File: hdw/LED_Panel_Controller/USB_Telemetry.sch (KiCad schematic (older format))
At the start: 7 parts

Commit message: reworked some USB stuff
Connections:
- net POS12_SNS+ renamed POS5_USB_SNS+
- net POS12_SNS- renamed POS5_USB_SNS-
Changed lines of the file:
@@
 $Descr A 11000 8500
 encoding utf-8
-Sheet 3 34
+Sheet 34 34
 Title "Pulse Oximeter"
 Date "2020-08-01"
@@
 $EndDescr
 Text GLabel 3790 1800 0    50   UnSpc ~ 0
-POS12_SNS+
+POS5_USB_SNS+
 Text GLabel 3790 2260 0    50   UnSpc ~ 0
-POS12_SNS-
+POS5_USB_SNS-
 $Comp
 L power:GND #PWR?
@@
 AR Path="/5EAE2D84/5E0ACFF2" Ref="#PWR?"  Part="1"
 AR Path="/5F581B58/5E0ACFF2" Ref="#PWR?"  Part="1"
+AR Path="/5F581BB7/5E0ACFF2" Ref="#PWR?"  Part="1"
+AR Path="/5F7B4289/5E0ACFF2" Ref="#PWR?"  Part="1"
 F 0 "#PWR?" H 5110 2190 50  0001 C CNN
 F 1 "GND" H 5110 2290 50  0000 C CNN
@@
 AR Path="/5EAE2D84/5E0AD665" Ref="#PWR?"  Part="1"
 AR Path="/5F581B58/5E0AD665" Ref="#PWR?"  Part="1"
+AR Path="/5F581BB7/5E0AD665" Ref="#PWR?"  Part="1"
+AR Path="/5F7B4289/5E0AD665" Ref="#PWR?"  Part="1"
 F 0 "#PWR?" H 5110 1490 50  0001 C CNN
 F 1 "+3.3V" H 5110 1780 50  0000 C CNN
@@
 AR Path="/5EAE2D84/5E0B2427" Ref="C?"  Part="1"
 AR Path="/5F581B58/5E0B2427" Ref="C?"  Part="1"
+AR Path="/5F581BB7/5E0B2427" Ref="C?"  Part="1"
+AR Path="/5F7B4289/5E0B2427" Ref="C?"  Part="1"
 F 0 "C?" H 5135 3110 50  0000 L CNN
 F 1 "0.1uF" H 5135 2910 50  0000 L CNN
@@
 AR Path="/5EAE2D84/5E0B535B" Ref="#PWR?"  Part="1"
 AR Path="/5F581B58/5E0B535B" Ref="#PWR?"  Part="1"
+AR Path="/5F581BB7/5E0B535B" Ref="#PWR?"  Part="1"
+AR Path="/5F7B4289/5E0B535B" Ref="#PWR?"  Part="1"
 F 0 "#PWR?" H 5110 2710 50  0001 C CNN
 F 1 "+3.3V" H 5110 3000 50  0000 C CNN
@@
 AR Path="/5EAE2D84/5E0B592B" Ref="#PWR?"  Part="1"
 AR Path="/5F581B58/5E0B592B" Ref="#PWR?"  Part="1"
+AR Path="/5F581BB7/5E0B592B" Ref="#PWR?"  Part="1"
+AR Path="/5F7B4289/5E0B592B" Ref="#PWR?"  Part="1"
 F 0 "#PWR?" H 5110 2910 50  0001 C CNN
 F 1 "GND" H 5110 3010 50  0000 C CNN
@@
 AR Path="/5EAE2D84/5E0B8BC8" Ref="DOC?"  Part="1"
 AR Path="/5F581B58/5E0B8BC8" Ref="DOC?"  Part="1"
+AR Path="/5F581BB7/5E0B8BC8" Ref="DOC?"  Part="1"
+AR Path="/5F7B4289/5E0B8BC8" Ref="DOC?"  Part="1"
 F 0 "DOC?" H 6010 3130 60  0001 C CNN
 F 1 "FIXME" H 5560 2880 60  0000 L CNN
@@
 AR Path="/5EAE2D84/5E2AA995" Ref="#PWR?"  Part="1"
 AR Path="/5F581B58/5E2AA995" Ref="#PWR?"  Part="1"
+AR Path="/5F581BB7/5E2AA995" Ref="#PWR?"  Part="1"
+AR Path="/5F7B4289/5E2AA995" Ref="#PWR?"  Part="1"
 F 0 "#PWR?" H 5110 4870 50  0001 C CNN
 F 1 "GND" H 5110 4970 50  0000 C CNN
@@
 AR Path="/5EAE2D84/5E2AA99A" Ref="#PWR?"  Part="1"
 AR Path="/5F581B58/5E2AA99A" Ref="#PWR?"  Part="1"
+AR Path="/5F581BB7/5E2AA99A" Ref="#PWR?"  Part="1"
+AR Path="/5F7B4289/5E2AA99A" Ref="#PWR?"  Part="1"
 F 0 "#PWR?" H 5110 3890 50  0001 C CNN
 F 1 "+3.3V" H 5110 4180 50  0000 C CNN
@@
 AR Path="/5EAE2D84/5E2AA99D" Ref="U?"  Part="1"
 AR Path="/5F581B58/5E2AA99D" Ref="U?"  Part="1"
+AR Path="/5F581BB7/5E2AA99D" Ref="U?"  Part="1"
+AR Path="/5F7B4289/5E2AA99D" Ref="U?"  Part="1"
 F 0 "U?" H 4860 4990 50  0000 C CNN
 F 1 "MCP9804" H 5510 4990 50  0000 C CNN
@@
 AR Path="/5EAE2D84/5E2AA9A1" Ref="C?"  Part="1"
 AR Path="/5F581B58/5E2AA9A1" Ref="C?"  Part="1"
+AR Path="/5F581BB7/5E2AA9A1" Ref="C?"  Part="1"
+AR Path="/5F7B4289/5E2AA9A1" Ref="C?"  Part="1"
 F 0 "C?" H 5135 5790 50  0000 L CNN
 F 1 "0.1uF" H 5135 5590 50  0000 L CNN
@@
 AR Path="/5EAE2D84/5E2AA9A6" Ref="#PWR?"  Part="1"
 AR Path="/5F581B58/5E2AA9A6" Ref="#PWR?"  Part="1"
+AR Path="/5F581BB7/5E2AA9A6" Ref="#PWR?"  Part="1"
+AR Path="/5F7B4289/5E2AA9A6" Ref="#PWR?"  Part="1"
 F 0 "#PWR?" H 5110 5390 50  0001 C CNN
 F 1 "+3.3V" H 5110 5680 50  0000 C CNN
@@
 AR Path="/5EAE2D84/5E2AA9AD" Ref="#PWR?"  Part="1"
 AR Path="/5F581B58/5E2AA9AD" Ref="#PWR?"  Part="1"
+AR Path="/5F581BB7/5E2AA9AD" Ref="#PWR?"  Part="1"
+AR Path="/5F7B4289/5E2AA9AD" Ref="#PWR?"  Part="1"
 F 0 "#PWR?" H 5110 5590 50  0001 C CNN
 F 1 "GND" H 5110 5690 50  0000 C CNN
@@
 AR Path="/5EAE2D84/5E2AA9AF" Ref="DOC?"  Part="1"
 AR Path="/5F581B58/5E2AA9AF" Ref="DOC?"  Part="1"
+AR Path="/5F581BB7/5E2AA9AF" Ref="DOC?"  Part="1"
+AR Path="/5F7B4289/5E2AA9AF" Ref="DOC?"  Part="1"
 F 0 "DOC?" H 6010 5810 60  0001 C CNN
 F 1 "FIXME" H 5560 5560 60  0000 L CNN
@@
 AR Path="/5EAE2D84/5E07E0FD" Ref="C?"  Part="1"
 AR Path="/5F581B58/5E07E0FD" Ref="C?"  Part="1"
+AR Path="/5F581BB7/5E07E0FD" Ref="C?"  Part="1"
+AR Path="/5F7B4289/5E07E0FD" Ref="C?"  Part="1"
 F 0 "C?" H 4255 2130 50  0000 L CNN
 F 1 "0.1uF" H 4255 1930 50  0000 L CNN

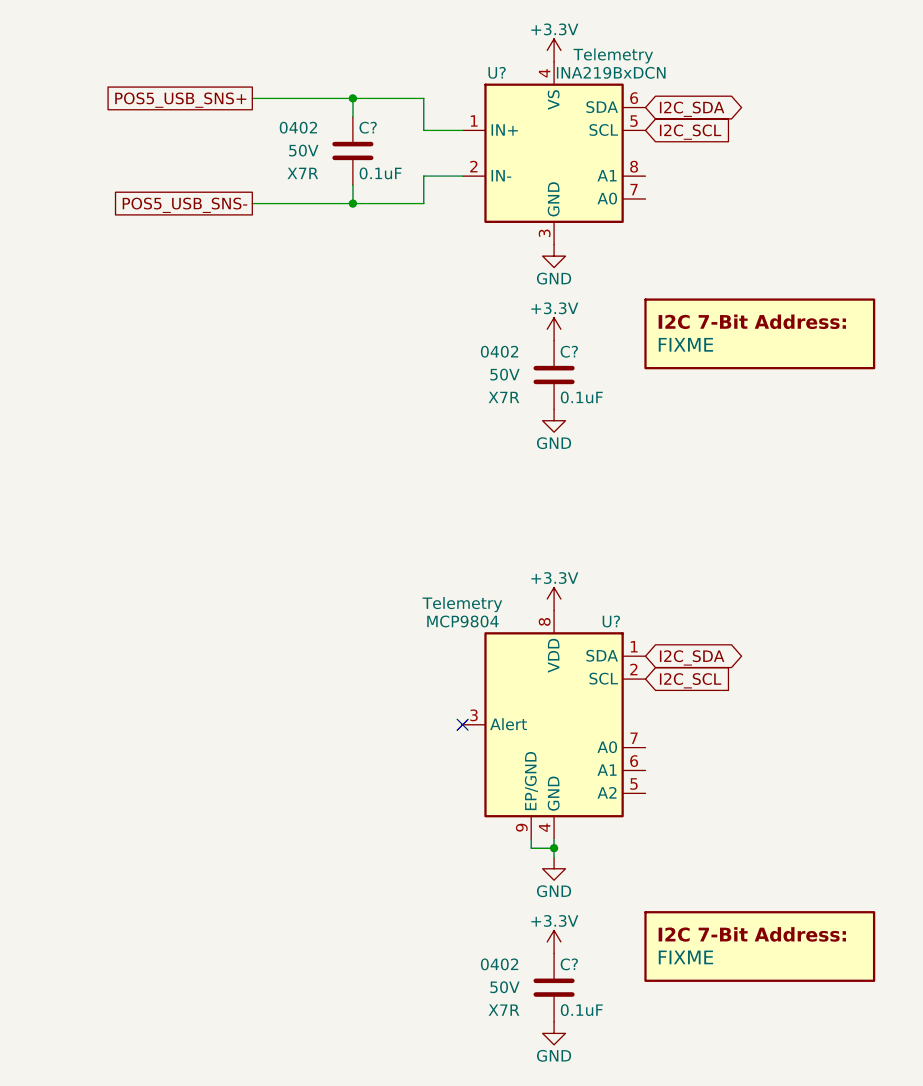
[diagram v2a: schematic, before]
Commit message: fixed level shifter sheet
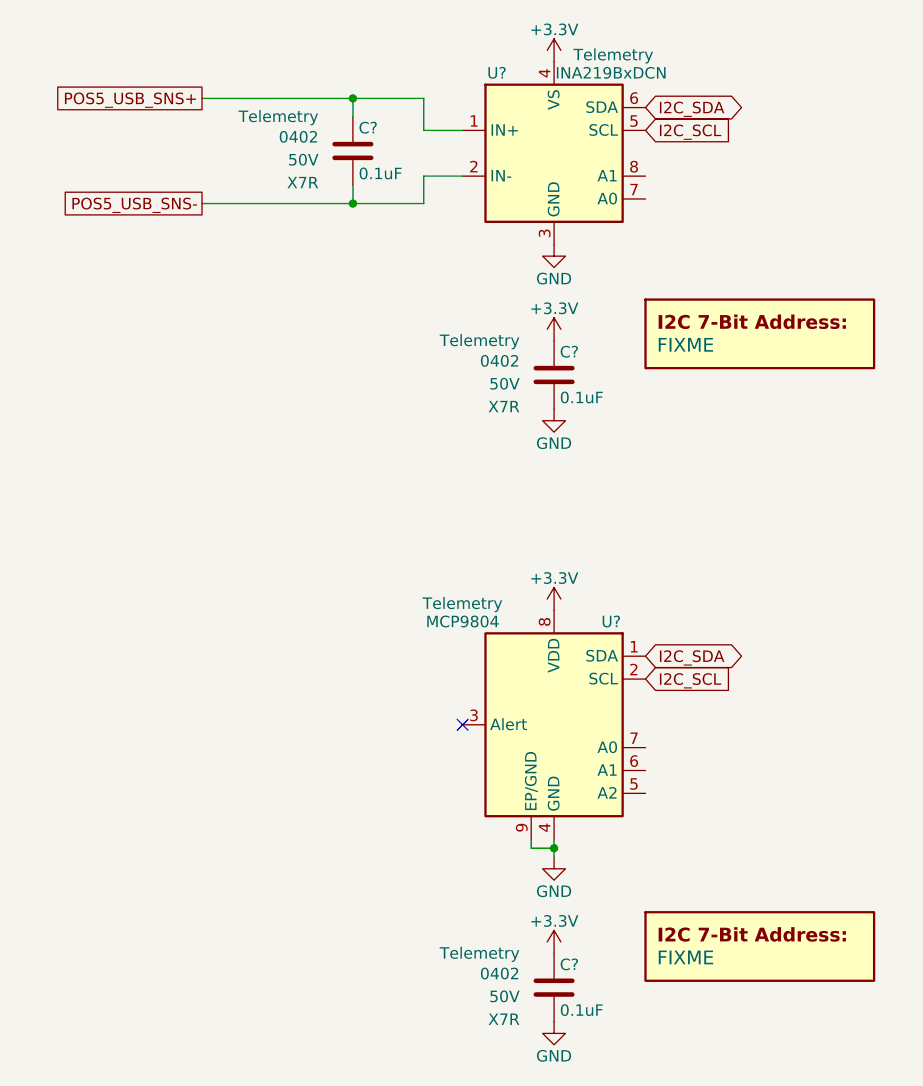
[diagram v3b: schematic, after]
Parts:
- removed C? (x3): 0.1uF, Capacitors_SMD:C_0402, symbol Custom_Library:C_Custom
- added C? (x3): 0.1uF, Capacitors_SMD:C_0402, symbol Custom_Library:C_Custom
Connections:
- net +3V3: now also C?.1, C?.1
- net GND: now also C?.2, C?.2
- net POS5_USB_SNS+: now also C?.1
- net POS5_USB_SNS-: now also C?.2
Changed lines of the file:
@@
 Comment4 ""
 $EndDescr
-Text GLabel 3790 1800 0    50   UnSpc ~ 0
+Text GLabel 3570 1800 0    50   UnSpc ~ 0
 POS5_USB_SNS+
-Text GLabel 3790 2260 0    50   UnSpc ~ 0
+Text GLabel 3570 2260 0    50   UnSpc ~ 0
 POS5_USB_SNS-
 $Comp
@@
 AR Path="/5EAE2D84/5E0ACFF2" Ref="#PWR?"  Part="1"
 AR Path="/5F581B58/5E0ACFF2" Ref="#PWR?"  Part="1"
-AR Path="/5F581BB7/5E0ACFF2" Ref="#PWR?"  Part="1"
+AR Path="/5F581B77/5E0ACFF2" Ref="#PWR?"  Part="1"
 AR Path="/5F7B4289/5E0ACFF2" Ref="#PWR?"  Part="1"
 F 0 "#PWR?" H 5110 2190 50  0001 C CNN
@@
 AR Path="/5EAE2D84/5E0AD665" Ref="#PWR?"  Part="1"
 AR Path="/5F581B58/5E0AD665" Ref="#PWR?"  Part="1"
-AR Path="/5F581BB7/5E0AD665" Ref="#PWR?"  Part="1"
+AR Path="/5F581B77/5E0AD665" Ref="#PWR?"  Part="1"
 AR Path="/5F7B4289/5E0AD665" Ref="#PWR?"  Part="1"
 F 0 "#PWR?" H 5110 1490 50  0001 C CNN
@@
 Text GLabel 5510 1940 2    50   Input ~ 0
 I2C_SCL
-$Comp
-L Custom_Library:C_Custom C?
-U 1 1 5E0B2427
-P 5110 3010
-AR Path="/5B3E071A/5E0B2427" Ref="C?"  Part="1"
-AR Path="/5E0652BA/5E0B2427" Ref="C?"  Part="1"
-AR Path="/5E0A0E29/5E0B2427" Ref="C?"  Part="1"
-AR Path="/5E052856/5E0B2427" Ref="C?"  Part="1"
-AR Path="/5EAE2D84/5E0B2427" Ref="C?"  Part="1"
-AR Path="/5F581B58/5E0B2427" Ref="C?"  Part="1"
-AR Path="/5F581BB7/5E0B2427" Ref="C?"  Part="1"
-AR Path="/5F7B4289/5E0B2427" Ref="C?"  Part="1"
-F 0 "C?" H 5135 3110 50  0000 L CNN
-F 1 "0.1uF" H 5135 2910 50  0000 L CNN
-F 2 "Capacitors_SMD:C_0402" H 5148 2860 50  0001 C CNN
-F 3 "" H 5135 3110 50  0001 C CNN
-F 4 "0402" H 4960 3110 50  0000 R CNN "display_footprint"
-F 5 "50V" H 4960 3010 50  0000 R CNN "Voltage"
-F 6 "X7R" H 4960 2910 50  0000 R CNN "Dielectric"
-F 7 "" H 1200 -3870 50  0001 C CNN "Digi-Key PN"
-	1    5110 3010
-	1    0    0    -1
-$EndComp
 $Comp
 L power:+3.3V #PWR?
@@
 AR Path="/5EAE2D84/5E0B535B" Ref="#PWR?"  Part="1"
 AR Path="/5F581B58/5E0B535B" Ref="#PWR?"  Part="1"
-AR Path="/5F581BB7/5E0B535B" Ref="#PWR?"  Part="1"
+AR Path="/5F581B77/5E0B535B" Ref="#PWR?"  Part="1"
 AR Path="/5F7B4289/5E0B535B" Ref="#PWR?"  Part="1"
 F 0 "#PWR?" H 5110 2710 50  0001 C CNN
@@
 AR Path="/5EAE2D84/5E0B592B" Ref="#PWR?"  Part="1"
 AR Path="/5F581B58/5E0B592B" Ref="#PWR?"  Part="1"
-AR Path="/5F581BB7/5E0B592B" Ref="#PWR?"  Part="1"
+AR Path="/5F581B77/5E0B592B" Ref="#PWR?"  Part="1"
 AR Path="/5F7B4289/5E0B592B" Ref="#PWR?"  Part="1"
 F 0 "#PWR?" H 5110 2910 50  0001 C CNN
@@
 AR Path="/5EAE2D84/5E0B8BC8" Ref="DOC?"  Part="1"
 AR Path="/5F581B58/5E0B8BC8" Ref="DOC?"  Part="1"
-AR Path="/5F581BB7/5E0B8BC8" Ref="DOC?"  Part="1"
+AR Path="/5F581B77/5E0B8BC8" Ref="DOC?"  Part="1"
 AR Path="/5F7B4289/5E0B8BC8" Ref="DOC?"  Part="1"
 F 0 "DOC?" H 6010 3130 60  0001 C CNN
@@
 AR Path="/5EAE2D84/5E2AA995" Ref="#PWR?"  Part="1"
 AR Path="/5F581B58/5E2AA995" Ref="#PWR?"  Part="1"
-AR Path="/5F581BB7/5E2AA995" Ref="#PWR?"  Part="1"
+AR Path="/5F581B77/5E2AA995" Ref="#PWR?"  Part="1"
 AR Path="/5F7B4289/5E2AA995" Ref="#PWR?"  Part="1"
 F 0 "#PWR?" H 5110 4870 50  0001 C CNN
@@
 AR Path="/5EAE2D84/5E2AA99A" Ref="#PWR?"  Part="1"
 AR Path="/5F581B58/5E2AA99A" Ref="#PWR?"  Part="1"
-AR Path="/5F581BB7/5E2AA99A" Ref="#PWR?"  Part="1"
+AR Path="/5F581B77/5E2AA99A" Ref="#PWR?"  Part="1"
 AR Path="/5F7B4289/5E2AA99A" Ref="#PWR?"  Part="1"
 F 0 "#PWR?" H 5110 3890 50  0001 C CNN
@@
 AR Path="/5EAE2D84/5E2AA99D" Ref="U?"  Part="1"
 AR Path="/5F581B58/5E2AA99D" Ref="U?"  Part="1"
-AR Path="/5F581BB7/5E2AA99D" Ref="U?"  Part="1"
+AR Path="/5F581B77/5E2AA99D" Ref="U?"  Part="1"
 AR Path="/5F7B4289/5E2AA99D" Ref="U?"  Part="1"
 F 0 "U?" H 4860 4990 50  0000 C CNN
@@
 NoConn ~ 4710 4540
 $Comp
-L Custom_Library:C_Custom C?
-U 1 1 5E2AA9A1
-P 5110 5690
-AR Path="/5B3E071A/5E2AA9A1" Ref="C?"  Part="1"
-AR Path="/5E0652BA/5E2AA9A1" Ref="C?"  Part="1"
-AR Path="/5E0A0E29/5E2AA9A1" Ref="C?"  Part="1"
-AR Path="/5E052856/5E2AA9A1" Ref="C?"  Part="1"
-AR Path="/5EAE2D84/5E2AA9A1" Ref="C?"  Part="1"
-AR Path="/5F581B58/5E2AA9A1" Ref="C?"  Part="1"
-AR Path="/5F581BB7/5E2AA9A1" Ref="C?"  Part="1"
-AR Path="/5F7B4289/5E2AA9A1" Ref="C?"  Part="1"
-F 0 "C?" H 5135 5790 50  0000 L CNN
-F 1 "0.1uF" H 5135 5590 50  0000 L CNN
-F 2 "Capacitors_SMD:C_0402" H 5148 5540 50  0001 C CNN
-F 3 "" H 5135 5790 50  0001 C CNN
-F 4 "0402" H 4960 5790 50  0000 R CNN "display_footprint"
-F 5 "50V" H 4960 5690 50  0000 R CNN "Voltage"
-F 6 "X7R" H 4960 5590 50  0000 R CNN "Dielectric"
-F 7 "" H 1200 -1190 50  0001 C CNN "Digi-Key PN"
-	1    5110 5690
-	1    0    0    -1
-$EndComp
-$Comp
 L power:+3.3V #PWR?
 U 1 1 5E2AA9A6
@@
 AR Path="/5EAE2D84/5E2AA9A6" Ref="#PWR?"  Part="1"
 AR Path="/5F581B58/5E2AA9A6" Ref="#PWR?"  Part="1"
-AR Path="/5F581BB7/5E2AA9A6" Ref="#PWR?"  Part="1"
+AR Path="/5F581B77/5E2AA9A6" Ref="#PWR?"  Part="1"
 AR Path="/5F7B4289/5E2AA9A6" Ref="#PWR?"  Part="1"
 F 0 "#PWR?" H 5110 5390 50  0001 C CNN
@@
 AR Path="/5EAE2D84/5E2AA9AD" Ref="#PWR?"  Part="1"
 AR Path="/5F581B58/5E2AA9AD" Ref="#PWR?"  Part="1"
-AR Path="/5F581BB7/5E2AA9AD" Ref="#PWR?"  Part="1"
+AR Path="/5F581B77/5E2AA9AD" Ref="#PWR?"  Part="1"
 AR Path="/5F7B4289/5E2AA9AD" Ref="#PWR?"  Part="1"
 F 0 "#PWR?" H 5110 5590 50  0001 C CNN
@@
 AR Path="/5EAE2D84/5E2AA9AF" Ref="DOC?"  Part="1"
 AR Path="/5F581B58/5E2AA9AF" Ref="DOC?"  Part="1"
-AR Path="/5F581BB7/5E2AA9AF" Ref="DOC?"  Part="1"
+AR Path="/5F581B77/5E2AA9AF" Ref="DOC?"  Part="1"
 AR Path="/5F7B4289/5E2AA9AF" Ref="DOC?"  Part="1"
 F 0 "DOC?" H 6010 5810 60  0001 C CNN
@@
 Wire Wire Line
 	4230 1880 4230 1800
-$Comp
-L Custom_Library:C_Custom C?
-U 1 1 5E07E0FD
-P 4230 2030
-AR Path="/5B3E071A/5E07E0FD" Ref="C?"  Part="1"
-AR Path="/5E0652BA/5E07E0FD" Ref="C?"  Part="1"
-AR Path="/5E0A0E29/5E07E0FD" Ref="C?"  Part="1"
-AR Path="/5E052856/5E07E0FD" Ref="C?"  Part="1"
-AR Path="/5EAE2D84/5E07E0FD" Ref="C?"  Part="1"
-AR Path="/5F581B58/5E07E0FD" Ref="C?"  Part="1"
-AR Path="/5F581BB7/5E07E0FD" Ref="C?"  Part="1"
-AR Path="/5F7B4289/5E07E0FD" Ref="C?"  Part="1"
-F 0 "C?" H 4255 2130 50  0000 L CNN
-F 1 "0.1uF" H 4255 1930 50  0000 L CNN
-F 2 "Capacitors_SMD:C_0402" H 4268 1880 50  0001 C CNN
-F 3 "" H 4255 2130 50  0001 C CNN
-F 4 "0402" H 4080 2130 50  0000 R CNN "display_footprint"
-F 5 "50V" H 4080 2030 50  0000 R CNN "Voltage"
-F 6 "X7R" H 4080 1930 50  0000 R CNN "Dielectric"
-F 7 "" H 320 -4850 50  0001 C CNN "Digi-Key PN"
-	1    4230 2030
-	1    0    0    -1
-$EndComp
-Wire Wire Line
-	3790 2260 4230 2260
-Wire Wire Line
-	3790 1800 4230 1800
 $Comp
 L Analog_ADC:INA219BxDCN U?
@@
 	4540 2260 4230 2260
 Connection ~ 4230 2260
+$Comp
+L Custom_Library:C_Custom C?
+U 1 1 6018BD18
+P 4230 2030
+AR Path="/5B3E071A/6018BD18" Ref="C?"  Part="1"
+AR Path="/5E0652BA/6018BD18" Ref="C?"  Part="1"
+AR Path="/5E0A0E29/6018BD18" Ref="C?"  Part="1"
+AR Path="/5E052856/6018BD18" Ref="C?"  Part="1"
+AR Path="/5EAE2D84/6018BD18" Ref="C?"  Part="1"
+AR Path="/5F581B58/6018BD18" Ref="C?"  Part="1"
+AR Path="/5F581B77/6018BD18" Ref="C?"  Part="1"
+AR Path="/5F7B4289/6018BD18" Ref="C?"  Part="1"
+F 0 "C?" H 4255 2130 50  0000 L CNN
+F 1 "0.1uF" H 4255 1930 50  0000 L CNN
+F 2 "Capacitors_SMD:C_0402" H 4268 1880 50  0001 C CNN
+F 3 "" H 4255 2130 50  0001 C CNN
+F 4 "0402" H 4080 2090 50  0000 R CNN "display_footprint"
+F 5 "50V" H 4080 1990 50  0000 R CNN "Voltage"
+F 6 "X7R" H 4080 1890 50  0000 R CNN "Dielectric"
+F 7 "Telemetry" H 4080 2180 50  0000 R CNN "Configuration"
+	1    4230 2030
+	1    0    0    -1
+$EndComp
+Wire Wire Line
+	3570 1800 4230 1800
+Wire Wire Line
+	3570 2260 4230 2260
+$Comp
+L Custom_Library:C_Custom C?
+U 1 1 6018C640
+P 5110 5690
+AR Path="/5B3E071A/6018C640" Ref="C?"  Part="1"
+AR Path="/5E0652BA/6018C640" Ref="C?"  Part="1"
+AR Path="/5E0A0E29/6018C640" Ref="C?"  Part="1"
+AR Path="/5E052856/6018C640" Ref="C?"  Part="1"
+AR Path="/5EAE2D84/6018C640" Ref="C?"  Part="1"
+AR Path="/5F581B58/6018C640" Ref="C?"  Part="1"
+AR Path="/5F581B77/6018C640" Ref="C?"  Part="1"
+AR Path="/5F7B4289/6018C640" Ref="C?"  Part="1"
+F 0 "C?" H 5135 5790 50  0000 L CNN
+F 1 "0.1uF" H 5135 5590 50  0000 L CNN
+F 2 "Capacitors_SMD:C_0402" H 5148 5540 50  0001 C CNN
+F 3 "" H 5135 5790 50  0001 C CNN
+F 4 "0402" H 4960 5750 50  0000 R CNN "display_footprint"
+F 5 "50V" H 4960 5650 50  0000 R CNN "Voltage"
+F 6 "X7R" H 4960 5550 50  0000 R CNN "Dielectric"
+F 7 "Telemetry" H 4960 5840 50  0000 R CNN "Configuration"
+	1    5110 5690
+	1    0    0    -1
+$EndComp
+$Comp
+L Custom_Library:C_Custom C?
+U 1 1 6018CFFA
+P 5110 3010
+AR Path="/5B3E071A/6018CFFA" Ref="C?"  Part="1"
+AR Path="/5E0652BA/6018CFFA" Ref="C?"  Part="1"
+AR Path="/5E0A0E29/6018CFFA" Ref="C?"  Part="1"
+AR Path="/5E052856/6018CFFA" Ref="C?"  Part="1"
+AR Path="/5EAE2D84/6018CFFA" Ref="C?"  Part="1"
+AR Path="/5F581B58/6018CFFA" Ref="C?"  Part="1"
+AR Path="/5F581B77/6018CFFA" Ref="C?"  Part="1"
+AR Path="/5F7B4289/6018CFFA" Ref="C?"  Part="1"
+F 0 "C?" H 5135 3110 50  0000 L CNN
+F 1 "0.1uF" H 5135 2910 50  0000 L CNN
+F 2 "Capacitors_SMD:C_0402" H 5148 2860 50  0001 C CNN
+F 3 "" H 5135 3110 50  0001 C CNN
+F 4 "0402" H 4960 3070 50  0000 R CNN "display_footprint"
+F 5 "50V" H 4960 2970 50  0000 R CNN "Voltage"
+F 6 "X7R" H 4960 2870 50  0000 R CNN "Dielectric"
+F 7 "Telemetry" H 4960 3160 50  0000 R CNN "Configuration"
+	1    5110 3010
+	1    0    0    -1
+$EndComp
 $EndSCHEMATC

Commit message: added digikey pns, footprints, bom scrubbed
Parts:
- C? (x3): Digi-Key PN (none) -> 490-10701-1-ND
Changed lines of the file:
@@
 F 6 "X7R" H 4080 1890 50  0000 R CNN "Dielectric"
 F 7 "Telemetry" H 4080 2180 50  0000 R CNN "Configuration"
+F 8 "490-10701-1-ND" H 4230 2030 50  0001 C CNN "Digi-Key PN"
 	1    4230 2030
 	1    0    0    -1
@@
 F 6 "X7R" H 4960 5550 50  0000 R CNN "Dielectric"
 F 7 "Telemetry" H 4960 5840 50  0000 R CNN "Configuration"
+F 8 "490-10701-1-ND" H 5110 5690 50  0001 C CNN "Digi-Key PN"
 	1    5110 5690
 	1    0    0    -1
@@
 F 6 "X7R" H 4960 2870 50  0000 R CNN "Dielectric"
 F 7 "Telemetry" H 4960 3160 50  0000 R CNN "Configuration"
+F 8 "490-10701-1-ND" H 5110 3010 50  0001 C CNN "Digi-Key PN"
 	1    5110 3010
 	1    0    0    -1
